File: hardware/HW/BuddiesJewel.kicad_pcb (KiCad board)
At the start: 2 copper layers, 25 parts, among them CON1 AVR-ISP6, CON2 ANTENNE, IC1 ATTINY25-P, P1 ALIM, U1 PT, U2 PT, U3 PT, U4 PT, U5 RF430CL330H

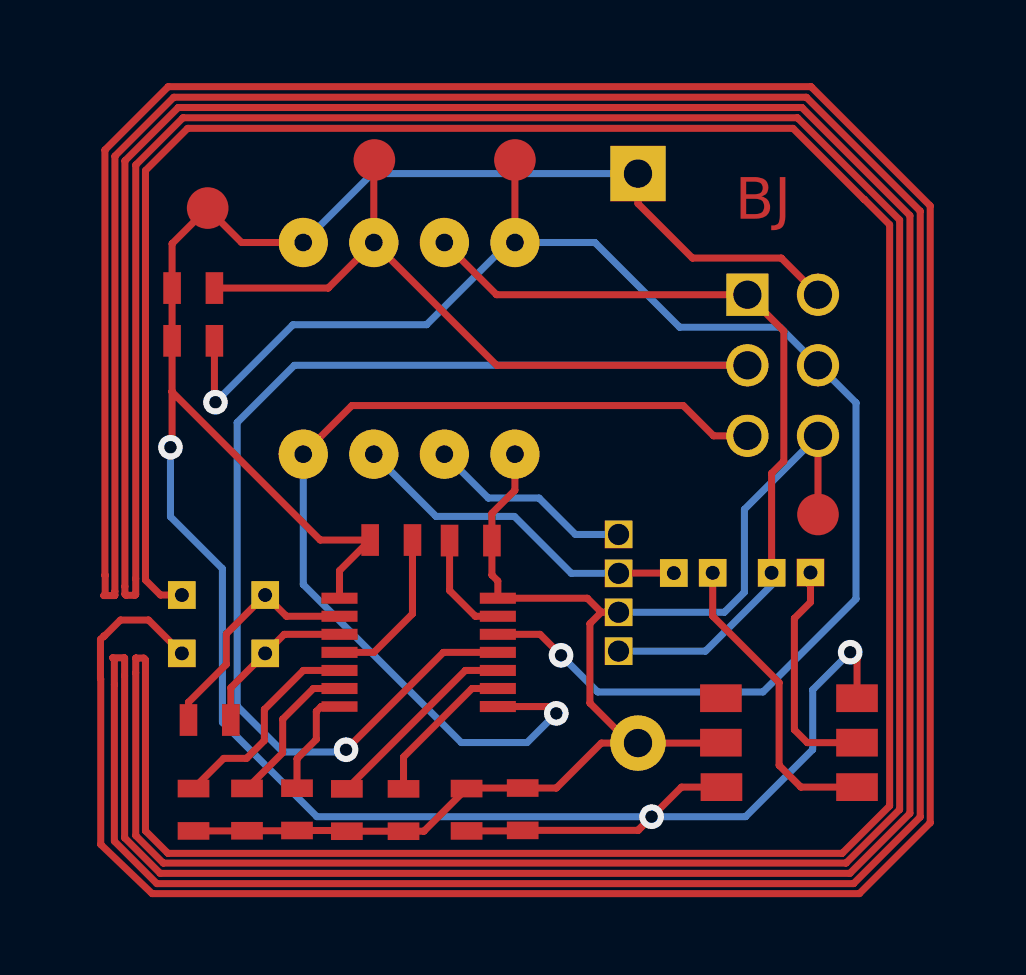
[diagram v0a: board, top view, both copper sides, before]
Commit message: change "RGB_LED (4)" D2 connector to "EXT_LED (3)" change ATtiny/RF430/WS2812/CON1 connections
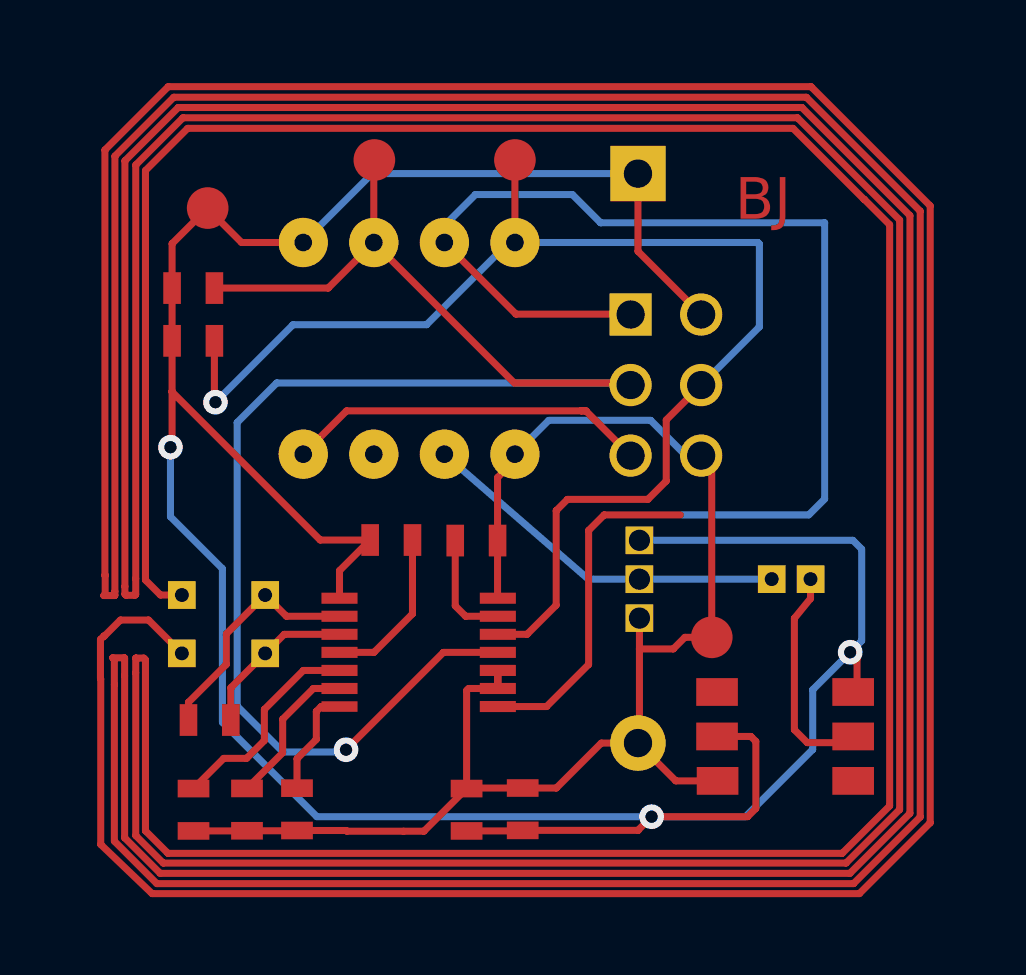
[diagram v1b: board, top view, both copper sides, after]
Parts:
- removed JP2: JUMPER, Jumper
- removed R7, R8: R, SM0603
- C1: value C -> 1 µF
- C2: value C -> 0,1 µF
- C3: value C -> 0,47 µF
- C4: value C -> 22 pF
- D2: value RGB_LED -> EXT_LED
- R1, R2, R3: value R -> not equipped
- R4, R5, R6: value R -> zero R
- moved U3 6.25 mm to (73.2, 47.2)
- moved CON1 4.27 mm to (71.6, 37.6)
- moved D2 4.06 mm to (70.6, 43.2), turned to 270 degrees
- moved D1 0.26 mm to (73.4, 48.6)
- moved JP1 0.24 mm to (76.8, 44.6)
- moved C3 0.20 mm to (64.7, 43.2)
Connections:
- CON1 pad 1: /PWM0/MISO -> /IT/MISO
- CON1 pad 5: /IT/RST -> /RST
- D1 pad 1: N-0000018 -> (no net)
- D1 pad 5: GND -> +3.3V
- D1 pad 6: +3.3V -> GND
- D2 pad 1: /PWM0/MISO -> +3.3V
- D2 pad 2: GND -> /LED_DI
- D2 pad 3: /PWM1 -> GND
- IC1 pad 1: /IT/RST -> /RST
- IC1 pad 2: /PWM1 -> (no net)
- IC1 pad 3: /PWM2 -> /LED_DI
- IC1 pad 6: /PWM0/MISO -> /IT/MISO
- JP1 pad 2: /PWM0/MISO -> /LED_DI
- U5 pad 10: N-000007 -> GND
- U5 pad 8: /IT/RST -> /IT/MISO
- U5 pad 9: N-000006 -> GND
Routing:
- net /IT/MISO: track 0.00 -> 50.5 mm
- net /IT/RST: track 36.0 -> 0.00 mm, vias 1 -> 0
- net /PWM0/MISO: track 29.4 -> 0.00 mm
- net /LED_DI: track 0.00 -> 13.5 mm
- net /RST: track 0.00 -> 13.3 mm
- net +3.3V: track 97.7 -> 110.9 mm
- net /PWM1: track 12.6 -> 0.00 mm
- net N-0000018: track 11.1 -> 0.00 mm
- net /SCL/SCK: track 65.7 -> 57.5 mm
- net /SDA/MOSI: track 55.2 -> 47.4 mm, vias 2 -> 1
- net /PWM2: track 7.47 -> 0.00 mm
- net N-000007: track 7.20 -> 0.00 mm
- net N-000006: track 5.56 -> 0.00 mm
- net GND: track 50.6 -> 53.9 mm

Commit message: new antenna and some enhanced stuff
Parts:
- moved R5 0.50 mm to (56.8, 52.5)
- moved R6 0.50 mm to (58.6, 52.5)
- moved C1 0.50 mm to (64.7, 52.5)
- moved R4 0.50 mm to (54.9, 52.5)
- moved R2 0.45 mm to (55.0, 36.2)
- moved R1 0.45 mm to (55.0, 34.3)
- moved D2 0.36 mm to (71.0, 43.1)
- moved U4 0.36 mm to (66.5, 29.4)
- moved CON1 0.36 mm to (71.9, 37.5)
- moved IC1 0.36 mm to (62.7, 36.2)
- moved R3 0.36 mm to (62.0, 43.1)
- moved U5 0.36 mm to (60.2, 45.2)
- moved U1 0.36 mm to (61.4, 29.4)
- moved U2 0.36 mm to (55.4, 31.2)
- moved C4 0.36 mm to (55.5, 49.6)
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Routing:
- net (no net): track 0.00 -> 328.2 mm, vias 0 -> 1
- net N-0000012: track 527.1 -> 256.2 mm, vias 0 -> 1
- net +3.3V: track 110.9 -> 115.6 mm
- net /IT/MISO: track 50.5 -> 47.9 mm, vias 0 -> 1

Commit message: new PCB revision
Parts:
- moved CON2 0.06 mm to (57.5, 45.0)
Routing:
- net N-0000012: track 256.2 -> 610.0 mm, vias 1 -> 2
- net (no net): track 328.2 -> 0.00 mm, vias 1 -> 0
